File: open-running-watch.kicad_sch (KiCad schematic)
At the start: 0 parts

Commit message: Add company name (using github URL), date, and change revision number to all schematic pages
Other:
- company: (none) -> github.com/fuad1502/open-running-watch-hw
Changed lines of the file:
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@@
 	(title_block
 		(title "Open Running Watch")
-		(rev "A")
+		(date "2024-04-12")
+		(rev "0.1.0")
+		(company "github.com/fuad1502/open-running-watch-hw")
 	)
 	(junction

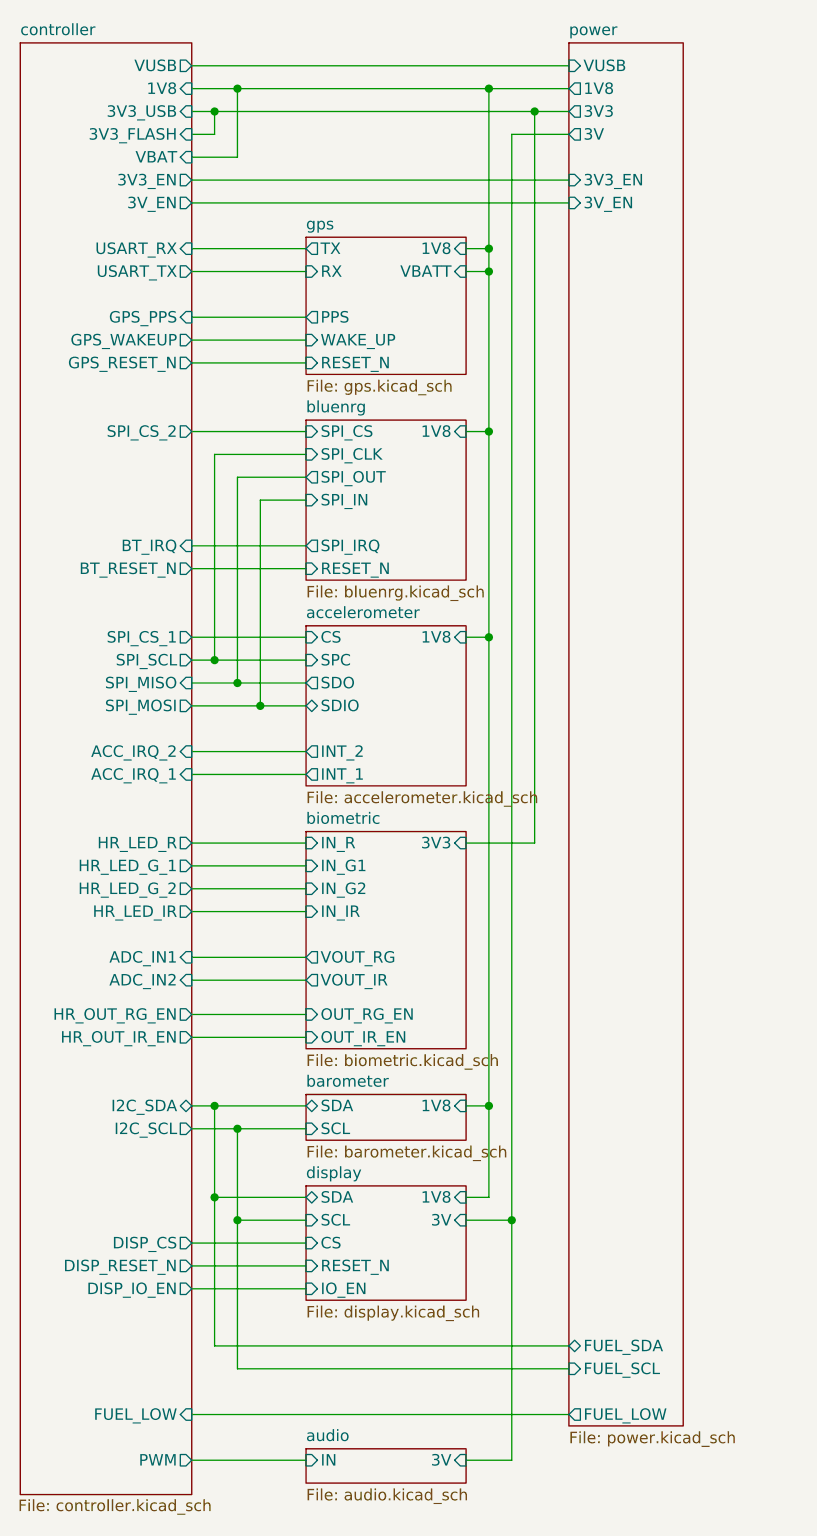
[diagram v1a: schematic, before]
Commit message: Changed display to 12616-06 Sharp MIP display with Azumo backlight
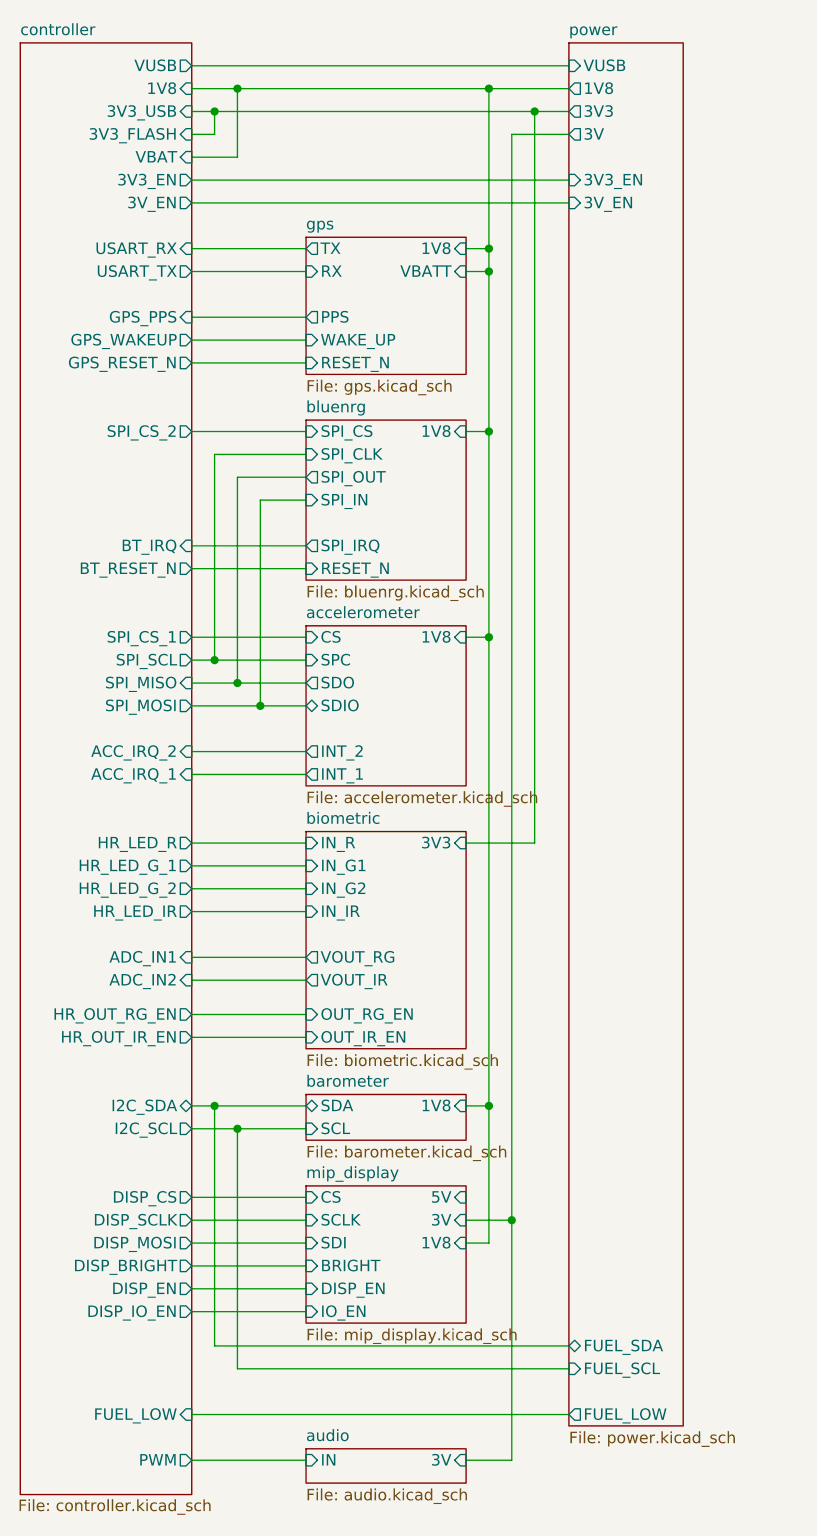
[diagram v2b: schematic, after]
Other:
- removed sheet display
- added sheet mip_display (mip_display.kicad_sch)
- sheet controller ports: added DISP_BRIGHT, DISP_EN, DISP_MOSI, DISP_SCLK; removed DISP_RESET_N

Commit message: Add 5V boost switching regulator
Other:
- sheet power ports: added 5V; removed none
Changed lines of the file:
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@@
+	(wire
+		(pts
+			(xy 105.41 38.1) (xy 104.14 38.1)
+		)
+		(stroke
+			(width 0)
+			(type default)
+		)
+	)
 	(wire
 		(pts
@@
 		(pts
 			(xy 63.5 133.35) (xy 76.2 133.35)
+		)
+		(stroke
+			(width 0)
+			(type default)
+		)
+	)
+	(wire
+		(pts
+			(xy 104.14 153.67) (xy 93.98 153.67)
+		)
+		(stroke
+			(width 0)
+			(type default)
+		)
+	)
+	(wire
+		(pts
+			(xy 104.14 38.1) (xy 104.14 153.67)
 		)
 		(stroke
@@
 			(effects
 				(font
+					(size 1.27 1.27)
+				)
+				(justify left)
+			)
+		)
+		(pin "5V" output
+			(at 105.41 38.1 180)
+			(effects
+				(font
